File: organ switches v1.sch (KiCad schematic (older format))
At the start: 21 parts, among them SW1 SW_SPST, SW10 SW_SPST, SW11 SW_SPST, SW12 SW_SPST, SW13 SW_SPST, SW14 SW_SPST, SW15 SW_SPST, SW16 SW_SPST, SW2 SW_SPST, SW3 SW_SPST, SW4 SW_SPST, SW5 SW_SPST, SW6 SW_SPST, SW7 SW_SPST, SW8 SW_SPST, SW9 SW_SPST, U1 SN74HC165DR, U2 SN74HC165DR

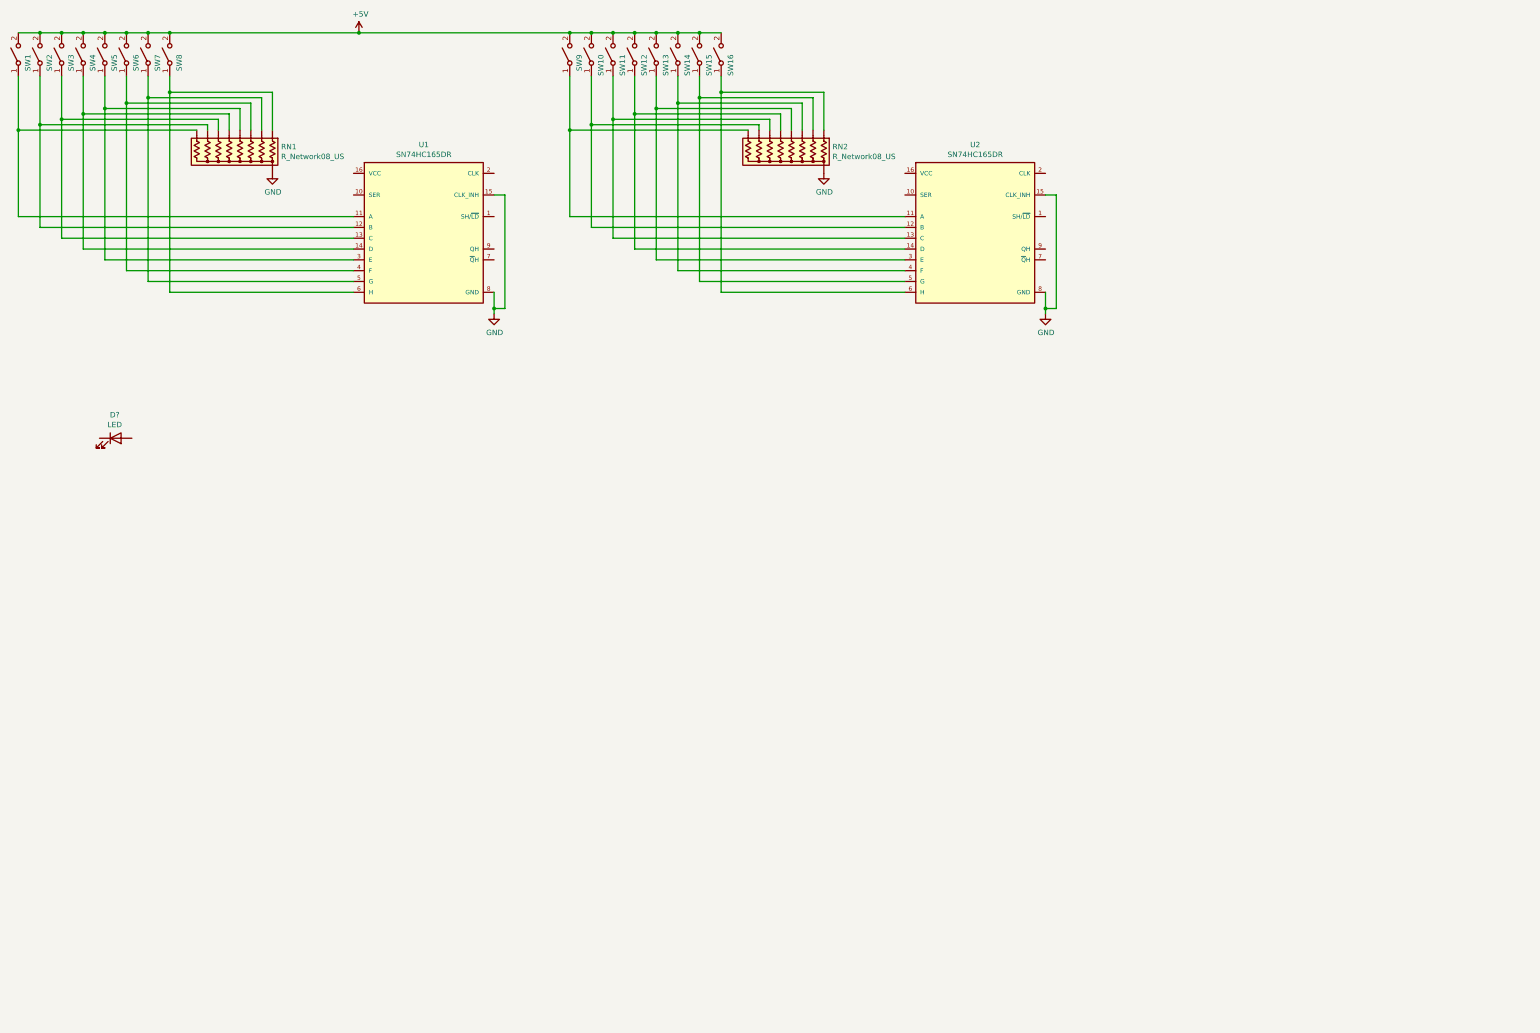
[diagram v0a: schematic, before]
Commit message: pcb component layout complete, no traces
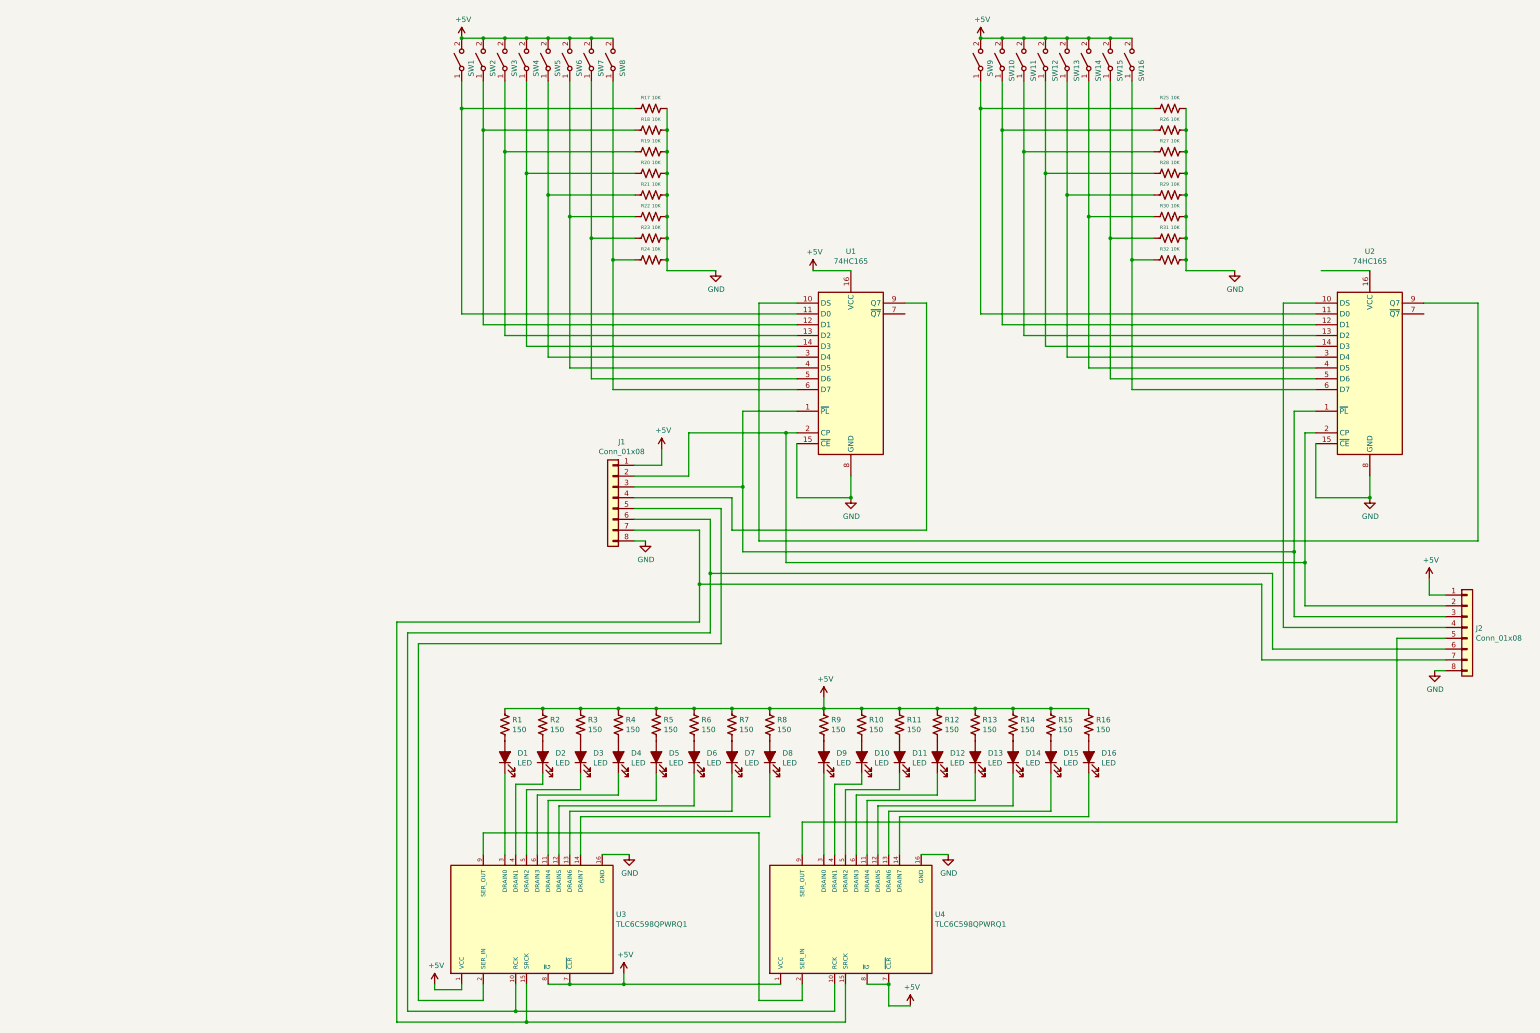
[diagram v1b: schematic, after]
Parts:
- removed D?: LED, symbol Device:LED
- removed RN1, RN2: R_Network08_US, Resistor_THT:R_Array_SIP9, symbol Device:R_Network08_US
- removed U1, U2: SN74HC165DR, eec:Texas_Instruments-D0016A-0-0-IPC_A, symbol eec:SN74HC165DR
- added D1, D10, D11, D12, D13, D14, D15, D16, D2, D3, D4, D5, D6, D7, D8, D9: LED, LED_THT:LED_D3.0mm, symbol Device:LED_ALT
- added J1, J2: Conn_01x08, Connector_PinHeader_2.54mm:PinHeader_1x08_P2.54mm_Vertical, symbol Connector_Generic:Conn_01x08
- added R1, R10, R11, R12, R13, R14, R15, R16, R2, R3, R4, R5, R6, R7, R8, R9: 150, Resistor_SMD:R_0603_1608Metric_Pad1.05x0.95mm_HandSolder, symbol Device:R_US
- added R17, R18, R19, R20, R21, R22, R23, R24, R25, R26, R27, R28, R29, R30, R31, R32: 10K, Resistor_SMD:R_0603_1608Metric_Pad1.05x0.95mm_HandSolder, symbol Device:R_US
- added U1, U2: 74HC165, eec:Texas_Instruments-D0016A-0-0-IPC_A, symbol 74xx:74HC165
- added U3, U4: TLC6C598QPWRQ1, eec:Texas_Instruments-PW0016A-0-0-0, symbol TLC6C598:TLC6C598QPWRQ1
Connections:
- net +5V: now also J1.1 (Pin_1), J2.1 (Pin_1), R1.1, R10.1, R11.1, R12.1, R13.1, R14.1, R15.1, R16.1, R2.1, R3.1, R4.1, R5.1, R6.1, R7.1, R8.1, R9.1, U1.16 (VCC), U3.1 (VCC), U3.7 (~CLR~), U3.8 (~G~), U4.1 (VCC), U4.7 (~CLR~), U4.8 (~G~)
- net GND: now also J1.8 (Pin_8), J2.8 (Pin_8), R17.1, R18.1, R19.1, R20.1, R21.1, R22.1, R23.1, R24.1, R25.1, R26.1, R27.1, R28.1, R29.1, R30.1, R31.1, R32.1, U1.15 (~CE), U1.8 (GND), U2.15 (~CE), U2.8 (GND), U3.16 (GND), U4.16 (GND)
- net at SW1.1 (A): now also R17.2, U1.11 (D0)
- net at SW2.1 (A): now also R18.2, U1.12 (D1)
- net at SW3.1 (A): now also R19.2, U1.13 (D2)
- net at SW4.1 (A): now also R20.2, U1.14 (D3)
- net at SW5.1 (A): now also R21.2, U1.3 (D4)
- net at SW6.1 (A): now also R22.2, U1.4 (D5)
- net at SW7.1 (A): now also R23.2, U1.5 (D6)
- net at SW8.1 (A): now also R24.2, U1.6 (D7)
- net at SW9.1 (A): now also R25.2, U2.11 (D0)
- net at SW16.1 (A): now also R32.2, U2.6 (D7)
- net at SW15.1 (A): now also R31.2, U2.5 (D6)
- net at SW14.1 (A): now also R30.2, U2.4 (D5)
- net at SW13.1 (A): now also R29.2, U2.3 (D4)
- net at SW12.1 (A): now also R28.2, U2.14 (D3)
- net at SW11.1 (A): now also R27.2, U2.13 (D2)
- net at SW10.1 (A): now also R26.2, U2.12 (D1)
- new net: J1.3 (Pin_3), J2.3 (Pin_3), U1.1 (~PL), U2.1 (~PL)
- new net: U1.10 (DS), U2.9 (Q7)
- new net: J1.2 (Pin_2), J2.2 (Pin_2), U1.2 (CP), U2.2 (CP)
- new net: J1.4 (Pin_4), U1.9 (Q7)
- new net: J2.4 (Pin_4), U2.10 (DS)
- new net: J2.5 (Pin_5), U4.9 (SER_OUT)
- new net: J1.6 (Pin_6), J2.6 (Pin_6), U3.10 (RCK), U4.10 (RCK)
- new net: J1.7 (Pin_7), J2.7 (Pin_7), U3.15 (SRCK), U4.15 (SRCK)
- new net: J1.5 (Pin_5), U3.2 (SER_IN)
- new net: D1.2 (A), R1.2
- new net: D1.1 (K), U3.3 (DRAIN0)
- new net: D2.2 (A), R2.2
- new net: D2.1 (K), U3.4 (DRAIN1)
- new net: D3.2 (A), R3.2
- new net: D3.1 (K), U3.5 (DRAIN2)
- new net: D4.2 (A), R4.2
- new net: D4.1 (K), U3.6 (DRAIN3)
- new net: D5.2 (A), R5.2
- new net: D5.1 (K), U3.11 (DRAIN4)
- new net: D6.2 (A), R6.2
- new net: D6.1 (K), U3.12 (DRAIN5)
- new net: D7.2 (A), R7.2
- new net: D7.1 (K), U3.13 (DRAIN6)
- new net: D8.2 (A), R8.2
- new net: D8.1 (K), U3.14 (DRAIN7)
- new net: U3.9 (SER_OUT), U4.2 (SER_IN)
- new net: D9.2 (A), R9.2
- new net: D9.1 (K), U4.3 (DRAIN0)
- new net: D10.2 (A), R10.2
- new net: D10.1 (K), U4.4 (DRAIN1)
- new net: D11.2 (A), R11.2
- new net: D11.1 (K), U4.5 (DRAIN2)
- new net: D12.2 (A), R12.2
- new net: D12.1 (K), U4.6 (DRAIN3)
- new net: D13.2 (A), R13.2
- new net: D13.1 (K), U4.11 (DRAIN4)
- new net: D14.2 (A), R14.2
- new net: D14.1 (K), U4.12 (DRAIN5)
- new net: D15.2 (A), R15.2
- new net: D15.1 (K), U4.13 (DRAIN6)
- new net: D16.2 (A), R16.2
- new net: D16.1 (K), U4.14 (DRAIN7)
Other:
- moved on the sheet: SW1, SW2, SW3, SW4, SW5, SW6, SW7, SW8

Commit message: addressed items 2, 5, 7, 9 from pinderh
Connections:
- net +5V: no longer U3.8 (~G~), U4.8 (~G~)
- net GND: now also U3.8 (~G~), U4.8 (~G~)
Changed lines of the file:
@@
 Connection ~ 6500 9600
-Wire Wire Line
-	5800 9600 6000 9600
-Connection ~ 6000 9600
-Wire Wire Line
-	8750 9600 8950 9600
-Connection ~ 8950 9600
 Wire Wire Line
 	8150 8100 13650 8100
@@
 Wire Wire Line
 	11200 2900 11200 4100
+$Comp
+L power:GND #PWR?
+U 1 1 5FF1BAA7
+P 5800 9650
+F 0 "#PWR?" H 5800 9400 50  0001 C CNN
+F 1 "GND" H 5805 9477 50  0000 C CNN
+F 2 "" H 5800 9650 50  0001 C CNN
+F 3 "" H 5800 9650 50  0001 C CNN
+	1    5800 9650
+	1    0    0    -1
+$EndComp
+Wire Wire Line
+	5800 9600 5800 9650
+$Comp
+L power:GND #PWR?
+U 1 1 5FF2DB3C
+P 8750 9650
+F 0 "#PWR?" H 8750 9400 50  0001 C CNN
+F 1 "GND" H 8755 9477 50  0000 C CNN
+F 2 "" H 8750 9650 50  0001 C CNN
+F 3 "" H 8750 9650 50  0001 C CNN
+	1    8750 9650
+	1    0    0    -1
+$EndComp
+Wire Wire Line
+	8750 9600 8750 9650
 $EndSCHEMATC
